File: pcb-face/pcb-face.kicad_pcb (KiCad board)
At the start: 2 copper layers, 84 x 84 mm, 4 parts

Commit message: added stepper motor spike (and heaps of other stuff)
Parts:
- added J1: Conn_02x02_Counter_Clockwise, Connector_PinHeader_2.54mm:PinHeader_2x02_P2.54mm_Vertical_SMD, B.Cu at (170.5, 70.3)
- added U1: SK6812, footprints:SK6812, B.Cu at (131.0, 94.0)
- added U2: SK6812, footprints:SK6812, B.Cu at (131.0, 107.0)
- added U3: SK6812, footprints:SK6812, B.Cu at (169.0, 107.0)
- added U4: SK6812, footprints:SK6812, B.Cu at (169.0, 94.0)
- moved REF** 32.6 mm to (137.0, 94.0)
- moved REF** 31.1 mm to (163.0, 107.0)
- moved REF** 16.3 mm to (137.0, 107.0)
- moved REF** 5.62 mm to (163.0, 94.0)
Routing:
- net +5V: track 0.00 -> 91.0 mm
- net Net-(U2-Pad4): track 0.00 -> 33.6 mm
- net Net-(J1-Pad3): track 0.00 -> 25.7 mm
- net Net-(U1-Pad4): track 0.00 -> 24.3 mm
- net Net-(U3-Pad4): track 0.00 -> 13.6 mm
- added copper zone on B.Cu, net GND
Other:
- outline, holes or cut-outs redrawn

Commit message: v1.0
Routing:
- added copper zone on F.Cu, net GND
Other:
- rule pad_to_mask_clearance: 0.051 -> 0
- board text added: "JLCJLCJLCJLC"
- board text added: "Motorcycle Tacho v1.0"

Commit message: add oshw logo
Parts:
- added G***: LOGO, footprints:OSHW, B.Cu at (150.0, 90.2)

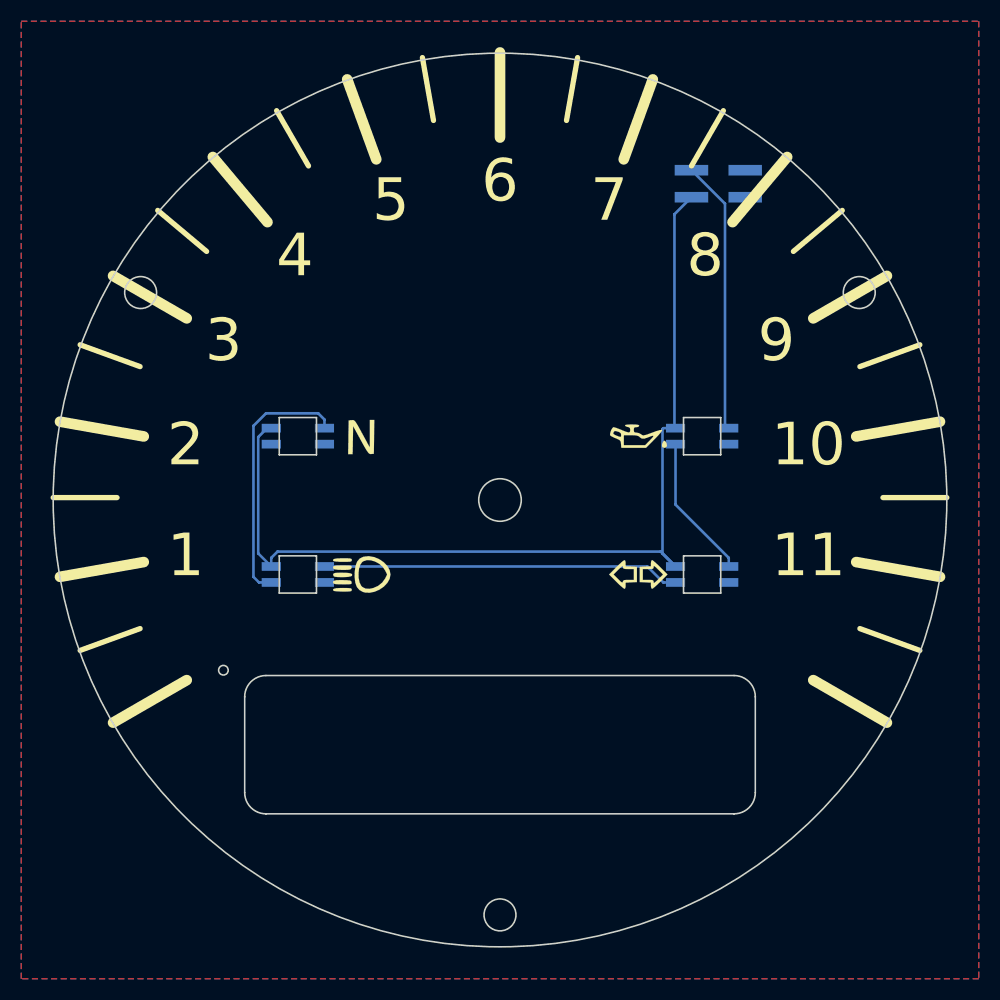
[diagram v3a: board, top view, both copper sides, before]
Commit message: made pcb bigger
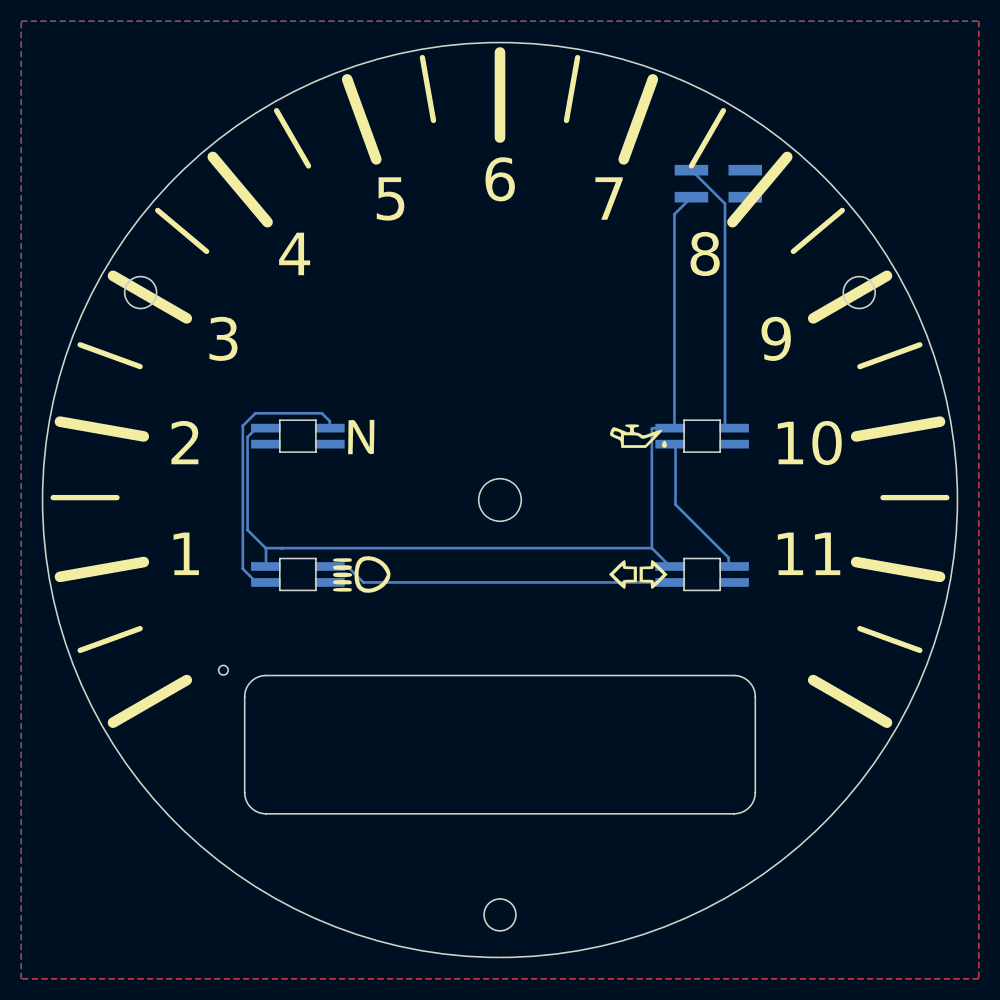
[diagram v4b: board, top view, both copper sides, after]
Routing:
- net Net-(U1-Pad4): track 24.3 -> 26.9 mm
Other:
- board size 84 x 84 mm -> 86 x 86 mm
- board text added: "5V"
- board text added: "DATA"
- board text added: "GND"

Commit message: started v1.1
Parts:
- removed G***: LOGO, footprints:OSHW
- removed J1: Conn_02x02_Counter_Clockwise, Connector_PinHeader_2.54mm:PinHeader_2x02_P2.54mm_Vertical_SMD
- removed U1, U2, U3, U4: SK6812, footprints:SK6812
- moved REF** 35.1 mm to (130.0, 95.0)
- moved REF** 34.8 mm to (170.0, 105.0)
- moved REF** 7.28 mm to (130.0, 105.0)
- moved REF** 7.07 mm to (170.0, 95.0)
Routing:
- net +5V: track 91.2 -> 0.00 mm
- net Net-(U2-Pad4): track 33.8 -> 0.00 mm
- net Net-(U1-Pad4): track 26.9 -> 0.00 mm
- net Net-(J1-Pad3): track 25.7 -> 0.00 mm
- net Net-(U3-Pad4): track 13.6 -> 0.00 mm
- removed copper zone on B.Cu, net GND
- removed copper zone on F.Cu, net GND
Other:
- outline, holes or cut-outs redrawn
- board text added: "Motorcycle Tacho v1.1"
- board text removed: "5V"
- board text removed: "DATA"
- board text removed: "GND"
- board text removed: "Motorcycle Tacho v1.0"

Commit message: v1.1
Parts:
- added G***: LOGO, footprints:OSHW, F.Cu at (150.0, 110.0)
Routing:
- net (no net): track 0.00 -> 2.00 mm
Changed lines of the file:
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@@
     (thickness 1.6)
     (drawings 56)
-    (tracks 0)
+    (tracks 2)
     (zones 0)
-    (modules 4)
+    (modules 5)
     (nets 1)
   )
@@
     (visible_elements 7FF9FFFF)
     (pcbplotparams
-      (layerselection 0x01070_fffffffe)
+      (layerselection 0x010f0_ffffffff)
       (usegerberextensions false)
       (usegerberattributes true)
@@
     (uvia_dia 0.3)
     (uvia_drill 0.1)
+  )
+  (module footprints:OSHW (layer F.Cu)
+    (at 150 110)
+    (fp_text reference G*** (at 0 0) (layer F.SilkS) hide
+      (effects (font (size 1.524 1.524) (thickness 0.3)))
+    )
+    (fp_text value LOGO (at 0.75 0) (layer F.SilkS) hide
+      (effects (font (size 1.524 1.524) (thickness 0.3)))
+    )
+    (fp_poly (pts (xy 0.20526 -3.592883) (xy 0.385381 -3.580397) (xy 0.51573 -3.559594) (xy 0.571414 -3.53055)
+      (xy 0.587793 -3.45675) (xy 0.615992 -3.309364) (xy 0.651356 -3.113236) (xy 0.673433 -2.986242)
+      (xy 0.756091 -2.504311) (xy 1.139047 -2.348312) (xy 1.522004 -2.192314) (xy 1.959471 -2.493407)
+      (xy 2.142389 -2.616993) (xy 2.29531 -2.715998) (xy 2.399541 -2.77858) (xy 2.434787 -2.794499)
+      (xy 2.484927 -2.760943) (xy 2.584443 -2.672609) (xy 2.714952 -2.547995) (xy 2.858074 -2.405601)
+      (xy 2.995426 -2.263927) (xy 3.108626 -2.141473) (xy 3.179294 -2.056738) (xy 3.193713 -2.030704)
+      (xy 3.166959 -1.976284) (xy 3.094711 -1.859237) (xy 2.988994 -1.698501) (xy 2.89881 -1.566218)
+      (xy 2.603908 -1.139604) (xy 2.751292 -0.782192) (xy 2.826717 -0.606423) (xy 2.892073 -0.466815)
+      (xy 2.935109 -0.389282) (xy 2.939627 -0.383831) (xy 3.003576 -0.358286) (xy 3.142847 -0.322455)
+      (xy 3.334225 -0.281895) (xy 3.473883 -0.255925) (xy 3.967191 -0.168969) (xy 3.981288 0.388224)
+      (xy 3.989463 0.6216) (xy 3.990125 0.781956) (xy 3.968388 0.886044) (xy 3.909366 0.95062)
+      (xy 3.798173 0.992437) (xy 3.619921 1.028249) (xy 3.373533 1.072224) (xy 3.188754 1.107983)
+      (xy 3.04704 1.137848) (xy 2.972585 1.15664) (xy 2.967088 1.15921) (xy 2.940487 1.212517)
+      (xy 2.889516 1.330516) (xy 2.825741 1.484793) (xy 2.760727 1.64693) (xy 2.706039 1.788511)
+      (xy 2.67324 1.881118) (xy 2.673096 1.881592) (xy 2.671375 1.958078) (xy 2.712073 2.065374)
+      (xy 2.803027 2.219751) (xy 2.916589 2.387157) (xy 3.035539 2.56102) (xy 3.128935 2.705351)
+      (xy 3.184153 2.800213) (xy 3.193713 2.824823) (xy 3.160308 2.876987) (xy 3.072358 2.978611)
+      (xy 2.948257 3.111136) (xy 2.806401 3.256005) (xy 2.665185 3.394658) (xy 2.543005 3.508538)
+      (xy 2.458256 3.579085) (xy 2.432357 3.592927) (xy 2.376571 3.565953) (xy 2.259515 3.493443)
+      (xy 2.101032 3.388013) (xy 1.997061 3.31613) (xy 1.602043 3.039334) (xy 1.40183 3.141474)
+      (xy 1.277151 3.202881) (xy 1.194877 3.239299) (xy 1.180296 3.243615) (xy 1.155235 3.200355)
+      (xy 1.100003 3.082361) (xy 1.022122 2.907311) (xy 0.929115 2.692882) (xy 0.828503 2.456752)
+      (xy 0.727808 2.2166) (xy 0.634553 1.990102) (xy 0.556259 1.794938) (xy 0.500449 1.648784)
+      (xy 0.493787 1.630223) (xy 0.454986 1.504364) (xy 0.457705 1.437132) (xy 0.504179 1.395405)
+      (xy 0.509843 1.392183) (xy 0.773339 1.191924) (xy 0.961072 0.937469) (xy 1.067774 0.645274)
+      (xy 1.088173 0.331793) (xy 1.017 0.013483) (xy 0.97967 -0.074853) (xy 0.869956 -0.277665)
+      (xy 0.748599 -0.41842) (xy 0.582604 -0.529408) (xy 0.448219 -0.594982) (xy 0.137433 -0.683129)
+      (xy -0.182642 -0.676391) (xy -0.448219 -0.594982) (xy -0.656716 -0.486361) (xy -0.800828 -0.367304)
+      (xy -0.913546 -0.205516) (xy -0.97967 -0.074853) (xy -1.077607 0.241847) (xy -1.082486 0.558354)
+      (xy -0.999578 0.858215) (xy -0.834152 1.124973) (xy -0.591478 1.342174) (xy -0.509843 1.392183)
+      (xy -0.459779 1.433301) (xy -0.453648 1.49728) (xy -0.489216 1.617241) (xy -0.493787 1.630223)
+      (xy -0.545064 1.766368) (xy -0.620093 1.954505) (xy -0.711352 2.176957) (xy -0.811319 2.416045)
+      (xy -0.912473 2.654093) (xy -1.00729 2.873421) (xy -1.08825 3.056353) (xy -1.147829 3.18521)
+      (xy -1.178506 3.242314) (xy -1.180296 3.243615) (xy -1.233643 3.222966) (xy -1.343329 3.170879)
+      (xy -1.399919 3.142449) (xy -1.598219 3.041284) (xy -1.994116 3.317106) (xy -2.168117 3.435527)
+      (xy -2.312382 3.528496) (xy -2.406979 3.583439) (xy -2.431324 3.592927) (xy -2.481687 3.559587)
+      (xy -2.584763 3.469626) (xy -2.723848 3.33813) (xy -2.833174 3.229966) (xy -2.983706 3.074546)
+      (xy -3.10341 2.943581) (xy -3.17729 2.853918) (xy -3.193713 2.824823) (xy -3.16672 2.768196)
+      (xy -3.094155 2.650422) (xy -2.988641 2.491438) (xy -2.916589 2.387157) (xy -2.780024 2.183665)
+      (xy -2.699952 2.040207) (xy -2.668538 1.940513) (xy -2.673096 1.881592) (xy -2.704752 1.792254)
+      (xy -2.758564 1.652752) (xy -2.823007 1.491506) (xy -2.886555 1.336938) (xy -2.937685 1.217468)
+      (xy -2.964869 1.161519) (xy -2.965306 1.160993) (xy -3.015656 1.146656) (xy -3.140115 1.118881)
+      (xy -3.314758 1.082927) (xy -3.371751 1.071648) (xy -3.574089 1.031721) (xy -3.750485 0.996492)
+      (xy -3.86814 0.972522) (xy -3.881484 0.96971) (xy -3.930834 0.955147) (xy -3.962802 0.924656)
+      (xy -3.980477 0.86024) (xy -3.986948 0.743903) (xy -3.985304 0.557648) (xy -3.981288 0.388224)
+      (xy -3.967191 -0.168969) (xy -3.473883 -0.255925) (xy -3.261277 -0.29659) (xy -3.085863 -0.336097)
+      (xy -2.970855 -0.368889) (xy -2.939627 -0.383831) (xy -2.902075 -0.447074) (xy -2.839899 -0.577238)
+      (xy -2.765307 -0.748485) (xy -2.750612 -0.783842) (xy -2.602547 -1.142904) (xy -2.89813 -1.569301)
+      (xy -3.020793 -1.749776) (xy -3.118596 -1.900382) (xy -3.179489 -2.002155) (xy -3.193713 -2.03456)
+      (xy -3.160067 -2.085521) (xy -3.071488 -2.185649) (xy -2.946514 -2.316563) (xy -2.803681 -2.459882)
+      (xy -2.661528 -2.597225) (xy -2.538592 -2.710211) (xy -2.453411 -2.780459) (xy -2.427306 -2.794499)
+      (xy -2.371892 -2.767695) (xy -2.253825 -2.695239) (xy -2.091967 -2.589067) (xy -1.952672 -2.494141)
+      (xy -1.518523 -2.193783) (xy -0.756091 -2.504311) (xy -0.673434 -2.986242) (xy -0.636042 -3.199323)
+      (xy -0.603099 -3.378152) (xy -0.579261 -3.497884) (xy -0.571414 -3.53055) (xy -0.515507 -3.559652)
+      (xy -0.385015 -3.580436) (xy -0.204809 -3.592902) (xy 0.00024 -3.59705) (xy 0.20526 -3.592883)) (layer F.SilkS) (width 0.01))
   )
   (module footprints:Turn_Signals (layer F.Cu)
@@
   )
   (gr_circle (center 150 100) (end 193 100) (layer Edge.Cuts) (width 0.15))
+  (segment (start 149.5 141) (end 150.5 141) (width 0.25) (layer F.Cu) (net 0))
+  (segment (start 149.5 137) (end 150.5 137) (width 0.25) (layer B.Cu) (net 0))
 )

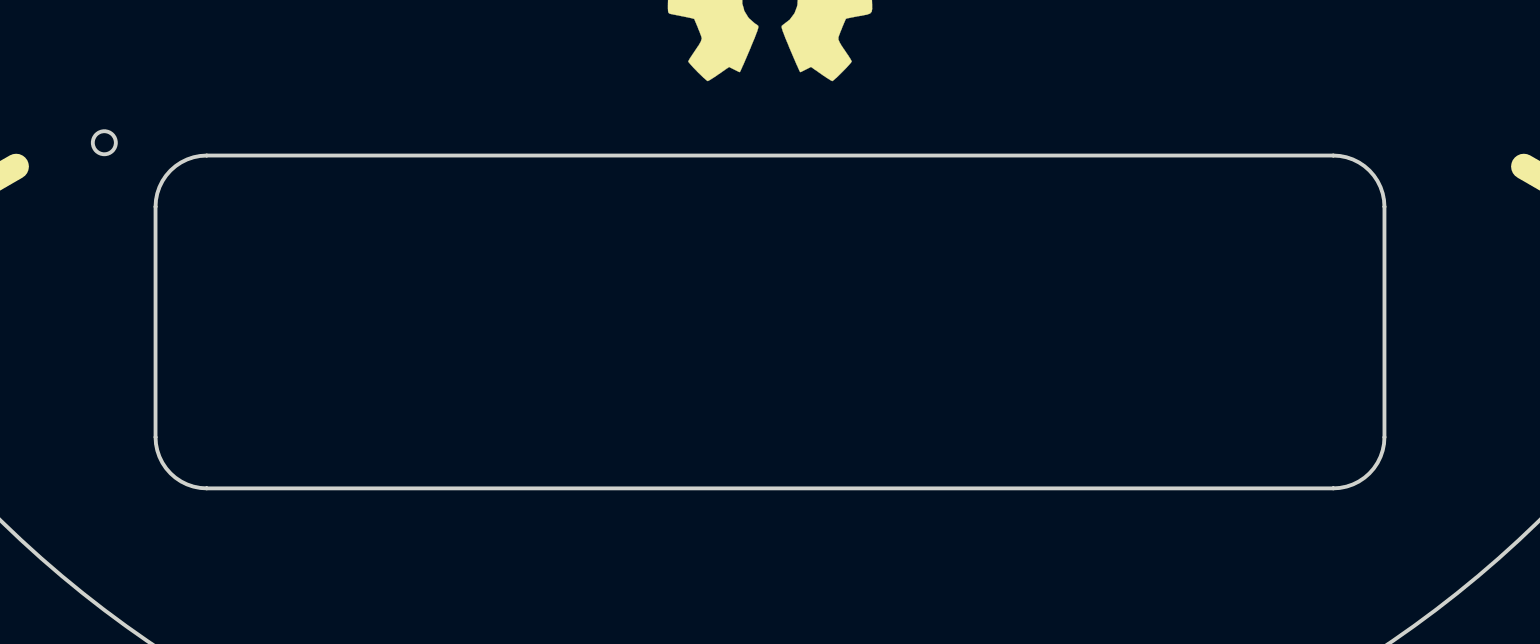
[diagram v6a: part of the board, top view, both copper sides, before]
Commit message: migrate to kicad 6
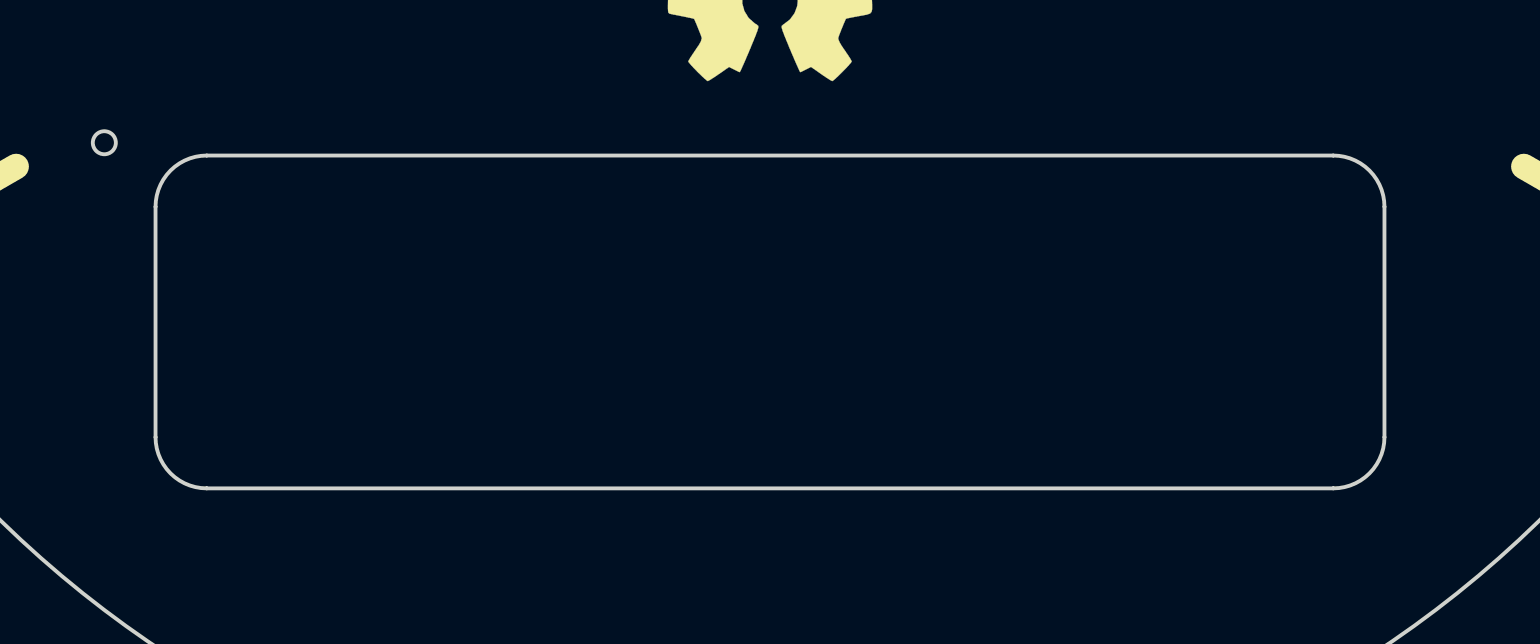
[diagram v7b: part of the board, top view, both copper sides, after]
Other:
- net class Default removed

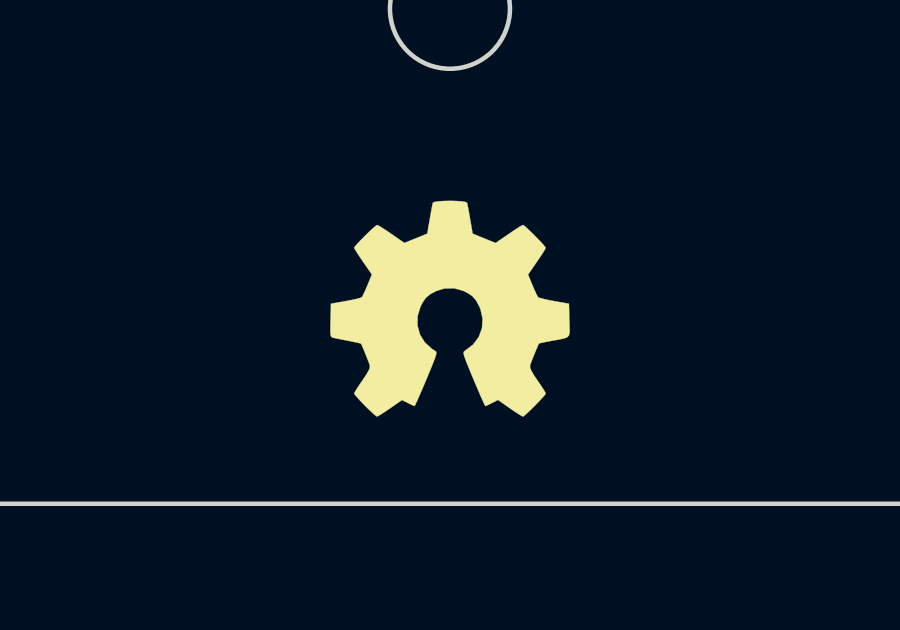
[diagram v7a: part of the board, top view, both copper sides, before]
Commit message: resolves #32: warning indicator symbol
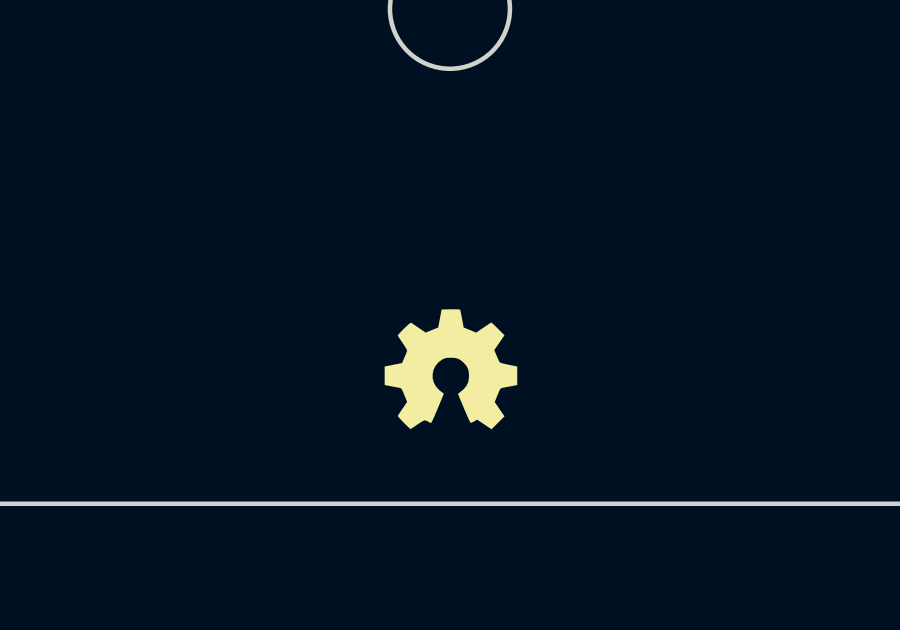
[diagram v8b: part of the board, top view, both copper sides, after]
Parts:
- REF**: value Oil_Pressure -> LOGO; footprint footprints:Oil_Pressure -> footprints:Warning
- REF**: value High_Beam -> LOGO
- REF**: value Neutral -> LOGO
- REF**: value Turn_Signals -> LOGO
- moved G*** 2.00 mm to (150.0, 112.0)
